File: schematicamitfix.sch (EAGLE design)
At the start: 41 parts, among them J1 FTDI_DEVICE, M1 WIRELESS-NRF24L01, U1 ATMEGA328P_TQFP, U2 GY-521MPU6050, U3 MAX1595EUA33+

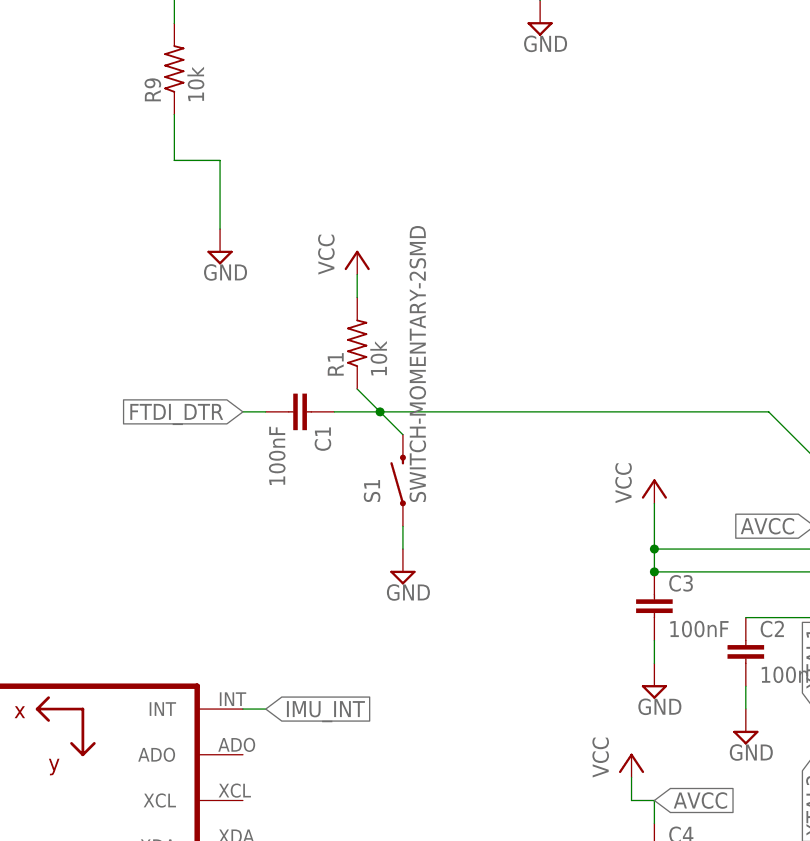
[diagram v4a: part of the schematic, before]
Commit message: Made push button library
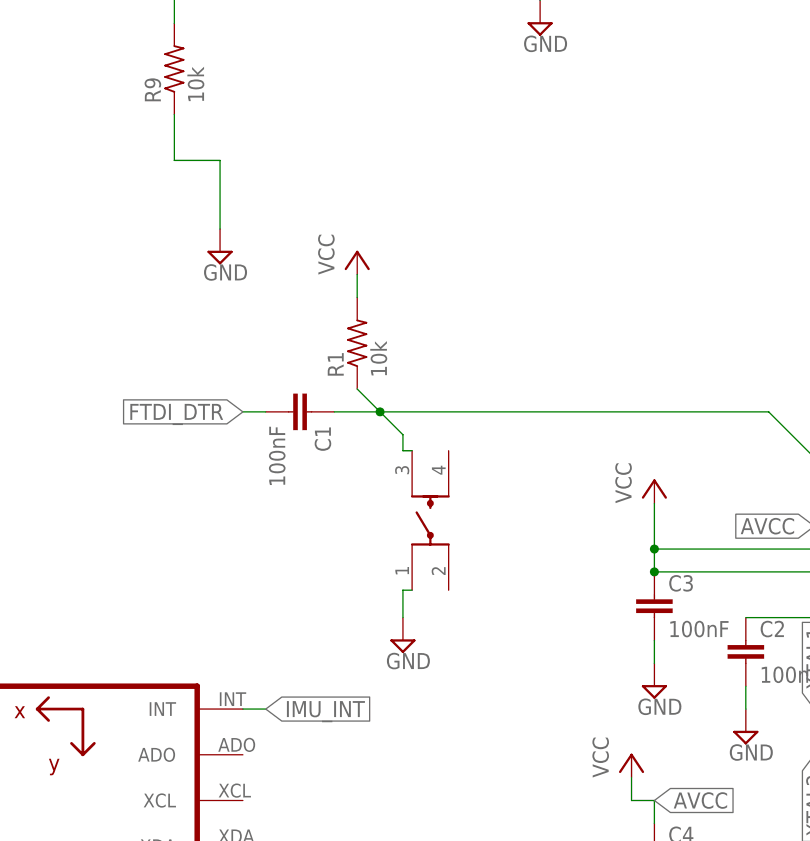
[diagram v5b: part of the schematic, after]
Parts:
- removed S1: SWITCH-MOMENTARY-2SMD, quad:SWITCH-MOMENTARY-2SMD
- added U$2: LL3301NF065QG, E-Switch:LL3301NF065QG
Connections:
- net GND: now also U$2.1; no longer S1.1
- net N$1: now also U$2.3; no longer S1.2
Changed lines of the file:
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@@
 <part name="SUPPLY6" library="supply2" library_urn="urn:adsk.eagle:library:372" deviceset="GND" device=""/>
 <part name="SUPPLY7" library="supply2" library_urn="urn:adsk.eagle:library:372" deviceset="GND" device=""/>
-<part name="S1" library="quad" deviceset="SWITCH-MOMENTARY-2" device="SMD"/>
 <part name="SUPPLY1" library="supply2" library_urn="urn:adsk.eagle:library:372" deviceset="GND" device=""/>
 <part name="R1" library="rcl" library_urn="urn:adsk.eagle:library:334" deviceset="R-US_" device="R0603" package3d_urn="urn:adsk.eagle:package:23555/2" value="10k"/>
@@
 <part name="C10" library="rcl" library_urn="urn:adsk.eagle:library:334" deviceset="C-EU" device="C0603" package3d_urn="urn:adsk.eagle:package:23616/2" value="0.47uF"/>
 <part name="C11" library="rcl" library_urn="urn:adsk.eagle:library:334" deviceset="C-EU" device="C0603" package3d_urn="urn:adsk.eagle:package:23616/2" value="100nF"/>
+<part name="U$2" library="E-Switch" deviceset="LL3301NF065QG" device=""/>
 </parts>
 <sheets>
@@
 <instance part="SUPPLY6" gate="GND" x="27.94" y="40.64"/>
 <instance part="SUPPLY7" gate="GND" x="17.78" y="45.72"/>
-<instance part="S1" gate="G$1" x="-10.16" y="68.58" rot="R90"/>
-<instance part="SUPPLY1" gate="GND" x="-10.16" y="58.42"/>
+<instance part="SUPPLY1" gate="GND" x="-10.16" y="50.8"/>
 <instance part="R1" gate="G$1" x="-15.24" y="83.82" rot="R90"/>
 <instance part="P+3" gate="VCC" x="-15.24" y="93.98"/>
@@
 <instance part="C10" gate="G$1" x="137.16" y="127"/>
 <instance part="C11" gate="G$1" x="132.08" y="144.78"/>
+<instance part="U$2" gate="A" x="-2.54" y="68.58" rot="R90"/>
 </instances>
 <busses>
@@
 </segment>
 <segment>
-<pinref part="S1" gate="G$1" pin="1"/>
-<wire x1="-10.16" y1="63.5" x2="-10.16" y2="60.96" width="0.1524" layer="91"/>
+<wire x1="-10.16" y1="56.388" x2="-10.16" y2="53.34" width="0.1524" layer="91"/>
 <pinref part="SUPPLY1" gate="GND" pin="GND"/>
+<pinref part="U$2" gate="A" pin="1"/>
+<wire x1="-9.144" y1="56.388" x2="-10.16" y2="56.388" width="0.1524" layer="91"/>
 </segment>
 </net>
@@
 <wire x1="30.48" y1="76.2" x2="-12.7" y2="76.2" width="0.1524" layer="91"/>
 <junction x="-12.7" y="76.2"/>
-<pinref part="S1" gate="G$1" pin="2"/>
 <wire x1="-10.16" y1="73.66" x2="-12.7" y2="76.2" width="0.1524" layer="91"/>
 <pinref part="R1" gate="G$1" pin="1"/>
@@
 <pinref part="C1" gate="G$1" pin="1"/>
 <wire x1="-12.7" y1="76.2" x2="-17.78" y2="76.2" width="0.1524" layer="91"/>
-</segment>
-</net>
+<pinref part="U$2" gate="A" pin="3"/>
+<wire x1="-9.144" y1="71.882" x2="-10.16" y2="71.882" width="0.1524" layer="91"/>
+<wire x1="-10.16" y1="71.882" x2="-10.16" y2="73.66" width="0.1524" layer="91"/>
+</segment>
+</net>

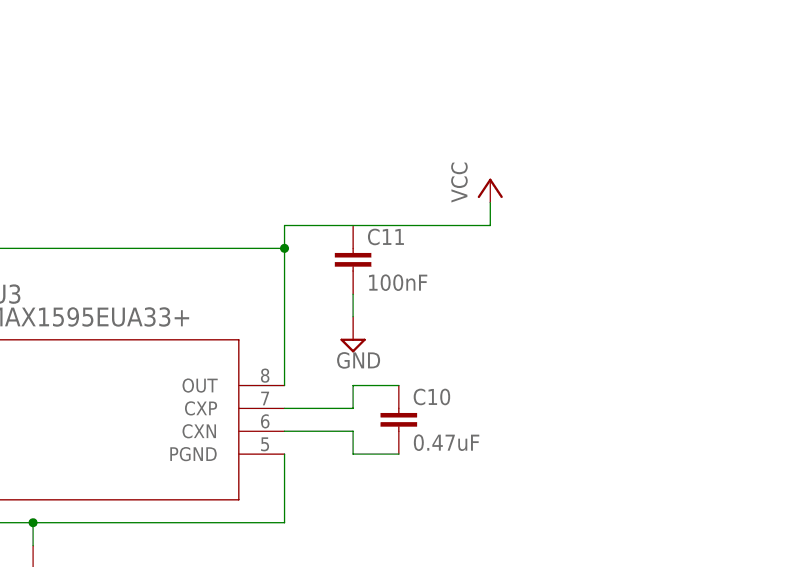
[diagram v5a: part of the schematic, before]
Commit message: Fixed capacitor value
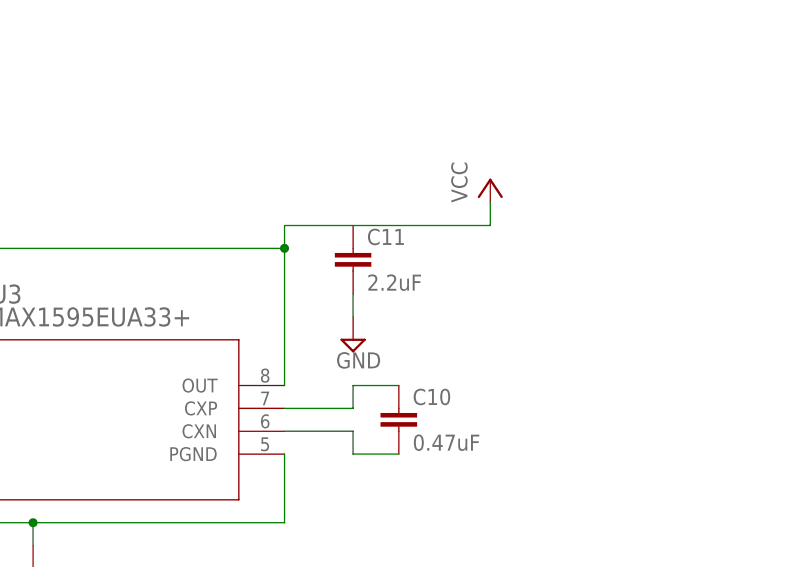
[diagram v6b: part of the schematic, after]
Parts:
- C11: value 100nF -> 2.2uF
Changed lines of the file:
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@@
 <part name="C9" library="rcl" library_urn="urn:adsk.eagle:library:334" deviceset="C-EU" device="C0603" package3d_urn="urn:adsk.eagle:package:23616/2" value="2.2uF"/>
 <part name="C10" library="rcl" library_urn="urn:adsk.eagle:library:334" deviceset="C-EU" device="C0603" package3d_urn="urn:adsk.eagle:package:23616/2" value="0.47uF"/>
-<part name="C11" library="rcl" library_urn="urn:adsk.eagle:library:334" deviceset="C-EU" device="C0603" package3d_urn="urn:adsk.eagle:package:23616/2" value="100nF"/>
+<part name="C11" library="rcl" library_urn="urn:adsk.eagle:library:334" deviceset="C-EU" device="C0603" package3d_urn="urn:adsk.eagle:package:23616/2" value="2.2uF"/>
 <part name="U$2" library="E-Switch" deviceset="LL3301NF065QG" device=""/>
 </parts>

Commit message: Fixed some stuff
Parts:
- removed U$16: N-CHANNEL-MOSFET-BSS138, quad:N-CHANNEL-MOSFET-BSS138
- added U$9: N-CHANNEL-MOSFET-IRLML6244TRPBF, quad:N-CHANNEL-MOSFET-IRLML6244TRPBF
- U$12, U$5, U$8: value N-CHANNEL-MOSFET-BSS138 -> N-CHANNEL-MOSFET-IRLML6244TRPBF; device quad:N-CHANNEL-MOSFET-BSS138 -> quad:N-CHANNEL-MOSFET-IRLML6244TRPBF
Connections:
- removed net N$28 (its old number): U$16.S
- new net N$30: U$9.S
- net N$13: now also U$8.D; no longer U$12.D
- net N$17: now also U$5.D; no longer U$16.D
- net N$19: now also C11.1
- net N$5: now also U$9.D; no longer U$5.D
- net N$9: now also U$12.D; no longer U$8.D
- net PWM1: now also U$12.G; no longer U$8.G
- net PWM2: now also U$9.G; no longer U$5.G
- net PWM3: now also U$8.G; no longer U$12.G
- net PWM4: now also U$5.G; no longer U$16.G
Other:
- moved on the sheet: C11, U$12, U$5, U$8

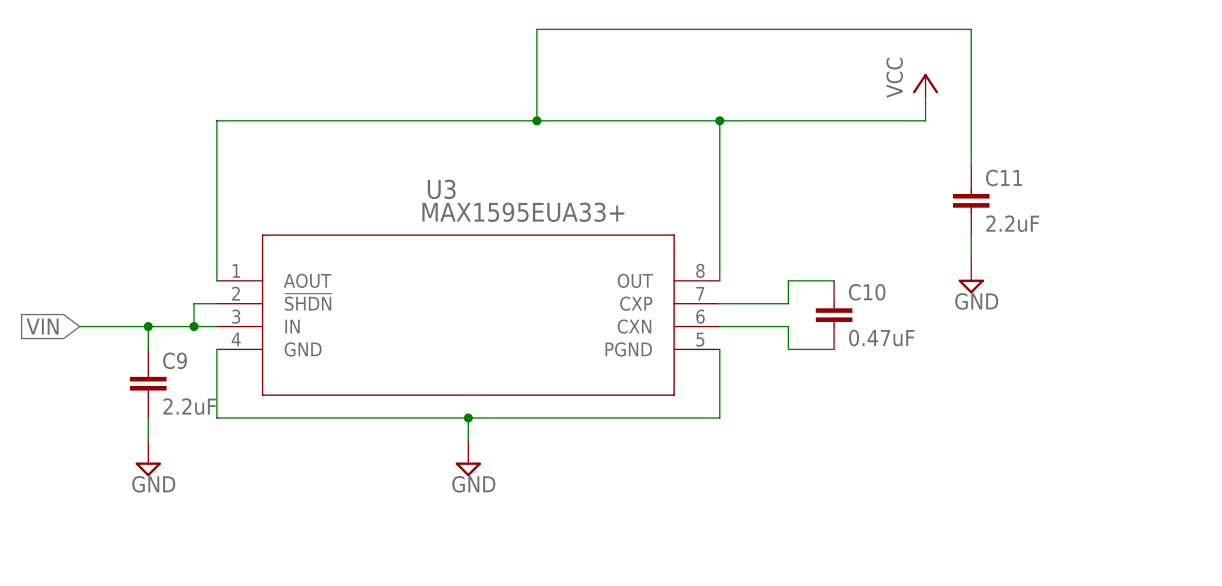
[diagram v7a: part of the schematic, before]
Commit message: Updated capacitors for voltage regulator
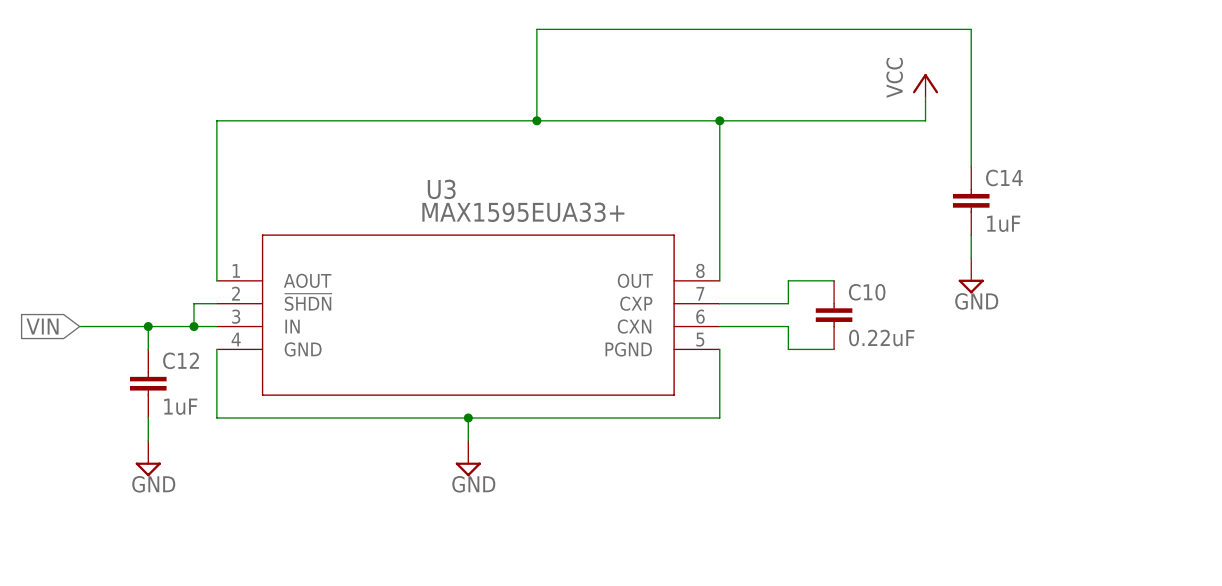
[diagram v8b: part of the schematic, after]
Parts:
- removed C11, C9: 2.2uF, rcl:C-EUC0603
- added C12, C14: 1uF, rcl:C-EUC0805
- C10: value 0.47uF -> 0.22uF
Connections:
- new net N$14: C12.2
- net GND: now also C14.2
- net N$19: now also C14.1; no longer C11.1
- net VIN: now also C12.1
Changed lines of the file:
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@@
 <part name="SUPPLY12" library="supply2" library_urn="urn:adsk.eagle:library:372" deviceset="GND" device=""/>
 <part name="P+7" library="supply1" library_urn="urn:adsk.eagle:library:371" deviceset="VCC" device=""/>
-<part name="C9" library="rcl" library_urn="urn:adsk.eagle:library:334" deviceset="C-EU" device="C0603" package3d_urn="urn:adsk.eagle:package:23616/2" value="2.2uF"/>
-<part name="C10" library="rcl" library_urn="urn:adsk.eagle:library:334" deviceset="C-EU" device="C0603" package3d_urn="urn:adsk.eagle:package:23616/2" value="0.47uF"/>
-<part name="C11" library="rcl" library_urn="urn:adsk.eagle:library:334" deviceset="C-EU" device="C0603" package3d_urn="urn:adsk.eagle:package:23616/2" value="2.2uF"/>
+<part name="C10" library="rcl" library_urn="urn:adsk.eagle:library:334" deviceset="C-EU" device="C0603" package3d_urn="urn:adsk.eagle:package:23616/2" value="0.22uF"/>
 <part name="U$2" library="E-Switch" deviceset="LL3301NF065QG" device=""/>
 <part name="U$5" library="quad" deviceset="N-CHANNEL-MOSFET" device="-IRLML6244TRPBF"/>
@@
 <part name="U$9" library="quad" deviceset="N-CHANNEL-MOSFET" device="-IRLML6244TRPBF"/>
 <part name="U$12" library="quad" deviceset="N-CHANNEL-MOSFET" device="-IRLML6244TRPBF"/>
+<part name="C12" library="rcl" library_urn="urn:adsk.eagle:library:334" deviceset="C-EU" device="C0805" package3d_urn="urn:adsk.eagle:package:23617/2" value="1uF"/>
+<part name="C14" library="rcl" library_urn="urn:adsk.eagle:library:334" deviceset="C-EU" device="C0805" package3d_urn="urn:adsk.eagle:package:23617/2" value="1uF"/>
 </parts>
 <sheets>
@@
 <instance part="SUPPLY12" gate="GND" x="152.4" y="129.54"/>
 <instance part="P+7" gate="VCC" x="147.32" y="152.4"/>
-<instance part="C9" gate="G$1" x="60.96" y="119.38"/>
 <instance part="C10" gate="G$1" x="137.16" y="127"/>
-<instance part="C11" gate="G$1" x="152.4" y="139.7"/>
 <instance part="U$2" gate="A" x="-2.54" y="68.58" rot="R90"/>
 <instance part="U$5" gate="G$1" x="246.38" y="-256.54"/>
@@
 <instance part="U$9" gate="G$1" x="246.38" y="25.4"/>
 <instance part="U$12" gate="G$1" x="276.86" y="165.1"/>
+<instance part="C12" gate="G$1" x="60.96" y="119.38"/>
+<instance part="C14" gate="G$1" x="152.4" y="139.7"/>
 </instances>
 <busses>
@@
 <wire x1="152.4" y1="134.62" x2="152.4" y2="132.08" width="0.1524" layer="91"/>
 <pinref part="SUPPLY12" gate="GND" pin="GND"/>
+<pinref part="C14" gate="G$1" pin="2"/>
 </segment>
 </net>
@@
 <junction x="60.96" y="124.46"/>
 <label x="53.34" y="124.46" size="1.778" layer="95" rot="R180" xref="yes"/>
+<pinref part="C12" gate="G$1" pin="1"/>
 </segment>
 </net>
@@
 <segment>
 <wire x1="60.96" y1="114.3" x2="60.96" y2="111.76" width="0.1524" layer="91"/>
+<pinref part="C12" gate="G$1" pin="2"/>
 </segment>
 </net>
@@
 <wire x1="68.58" y1="147.32" x2="104.14" y2="147.32" width="0.1524" layer="91"/>
 <junction x="124.46" y="147.32"/>
-<pinref part="C11" gate="G$1" pin="1"/>
 <wire x1="104.14" y1="147.32" x2="124.46" y2="147.32" width="0.1524" layer="91"/>
 <wire x1="152.4" y1="142.24" x2="152.4" y2="157.48" width="0.1524" layer="91"/>
@@
 <wire x1="104.14" y1="157.48" x2="104.14" y2="147.32" width="0.1524" layer="91"/>
 <junction x="104.14" y="147.32"/>
-</segment>
-</net>
+<pinref part="C14" gate="G$1" pin="1"/>
+</segment>
+</net>
